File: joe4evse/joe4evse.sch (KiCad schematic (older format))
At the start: 39 parts, among them J1 USB_B_Micro, J10 Conn_01x02, J11 Conn_01x02, J2 Conn_01x03, J3 Conn_01x03, J4 Conn_01x02, J5 Conn_01x03, J6 CONNFLY_Elec_DS1129-04-S8B0P-X, J7 8P8C_LED_Shielded, J9 Conn_01x02, Q1 AO3402, Q2 AO3402, Q3 AO3402, SW1 JS202011CQN, U1 CH340C, U2 MAX3485

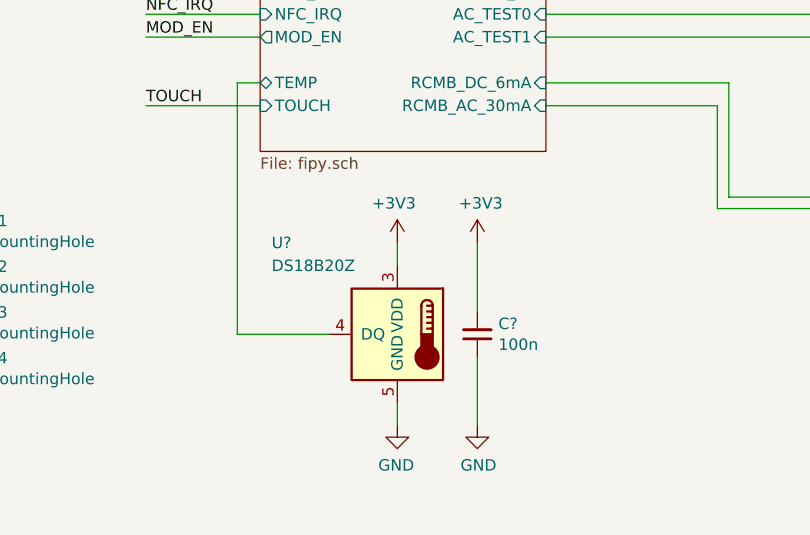
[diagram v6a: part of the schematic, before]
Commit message: joe: Add temperature sensor
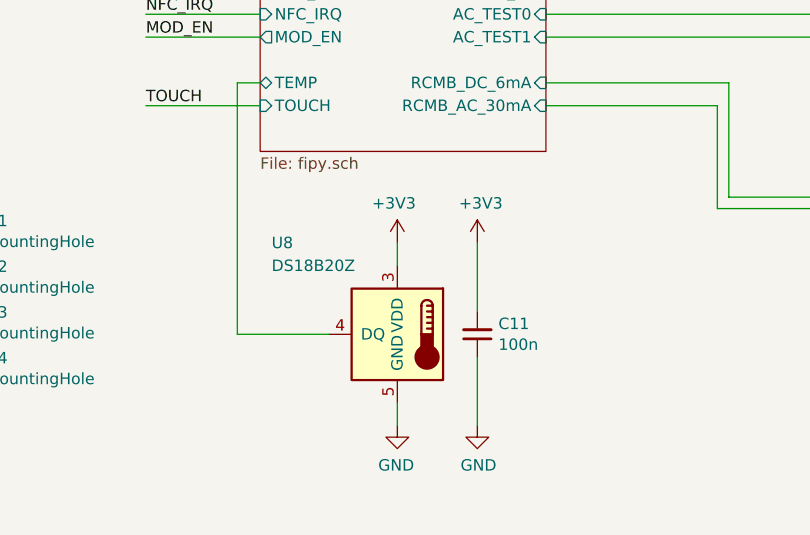
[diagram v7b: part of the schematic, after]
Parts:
- gave numbers to parts that had none: 2
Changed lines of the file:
@@
 	8700 5800 8800 5800
 $Comp
-L Sensor_Temperature:DS18B20Z U?
+L Sensor_Temperature:DS18B20Z U8
 U 1 1 5E547938
 P 5100 7000
-F 0 "U?" H 5650 7400 50  0000 R CNN
+F 0 "U8" H 5650 7400 50  0000 R CNN
 F 1 "DS18B20Z" H 5650 7300 50  0000 R CNN
 F 2 "Package_SO:SOIC-8_3.9x4.9mm_P1.27mm" H 4100 6750 50  0001 C CNN
@@
 $EndComp
 $Comp
-L power:+3V3 #PWR?
+L power:+3V3 #PWR066
 U 1 1 5E54C87A
 P 5100 6600
-F 0 "#PWR?" H 5100 6450 50  0001 C CNN
+F 0 "#PWR066" H 5100 6450 50  0001 C CNN
 F 1 "+3V3" H 5115 6773 50  0000 C CNN
 F 2 "" H 5100 6600 50  0001 C CNN
@@
 $EndComp
 $Comp
-L power:GND #PWR?
+L power:GND #PWR073
 U 1 1 5E54D1CF
 P 5100 7400
-F 0 "#PWR?" H 5100 7150 50  0001 C CNN
+F 0 "#PWR073" H 5100 7150 50  0001 C CNN
 F 1 "GND" H 5105 7227 50  0000 C CNN
 F 2 "" H 5100 7400 50  0001 C CNN
@@
 	5100 7400 5100 7300
 $Comp
-L Device:C_Small C?
+L Device:C_Small C11
 U 1 1 5E577814
 P 5450 7000
-F 0 "C?" H 5358 6954 50  0000 R CNN
+F 0 "C11" H 5358 6954 50  0000 R CNN
 F 1 "100n" H 5358 7045 50  0000 R CNN
 F 2 "Capacitor_SMD:C_0603_1608Metric" H 5450 7000 50  0001 C CNN
@@
 $EndComp
 $Comp
-L power:+3V3 #PWR?
+L power:+3V3 #PWR072
 U 1 1 5E57781A
 P 5450 6600
-F 0 "#PWR?" H 5450 6450 50  0001 C CNN
+F 0 "#PWR072" H 5450 6450 50  0001 C CNN
 F 1 "+3V3" H 5465 6773 50  0000 C CNN
 F 2 "" H 5450 6600 50  0001 C CNN
@@
 $EndComp
 $Comp
-L power:GND #PWR?
+L power:GND #PWR074
 U 1 1 5E577820
 P 5450 7400
-F 0 "#PWR?" H 5450 7150 50  0001 C CNN
+F 0 "#PWR074" H 5450 7150 50  0001 C CNN
 F 1 "GND" H 5455 7227 50  0000 C CNN
 F 2 "" H 5450 7400 50  0001 C CNN

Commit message: WIP: joe: Add errout signal
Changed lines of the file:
@@
 F21 "RCMB_DC_6mA" I R 5750 5900 50
 F22 "RCMB_AC_30mA" I R 5750 6000 50
+F23 "ERROUT" O R 5750 4800 50
 $EndSheet
 Wire Notes Line
